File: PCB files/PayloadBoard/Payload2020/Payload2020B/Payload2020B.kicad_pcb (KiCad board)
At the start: 2 copper layers, 50 x 150 mm, 3 parts, among them J1 BridgeConn, U1 Xbee_XBP9B, U2 BerryIMUv3

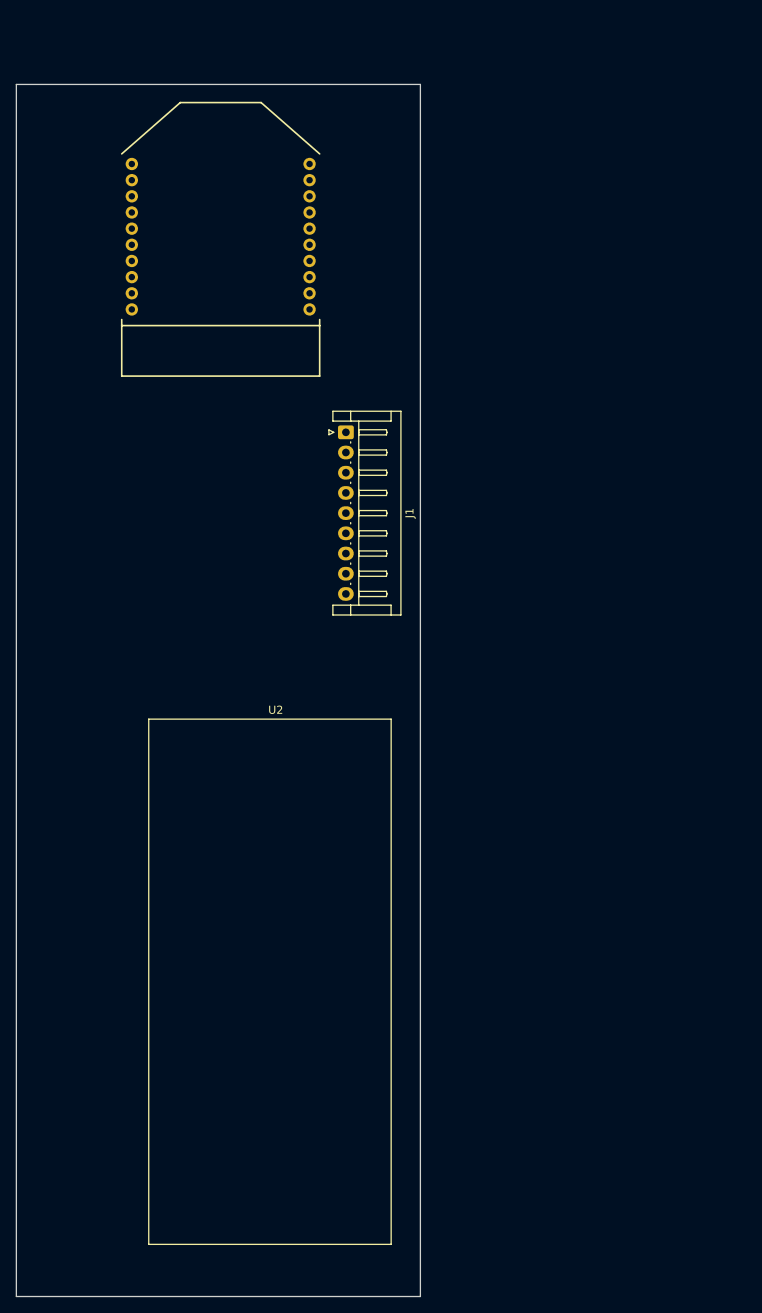
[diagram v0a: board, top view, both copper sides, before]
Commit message: Changed board sizes based on payload bay dimensions Changed battery connector to JST XH
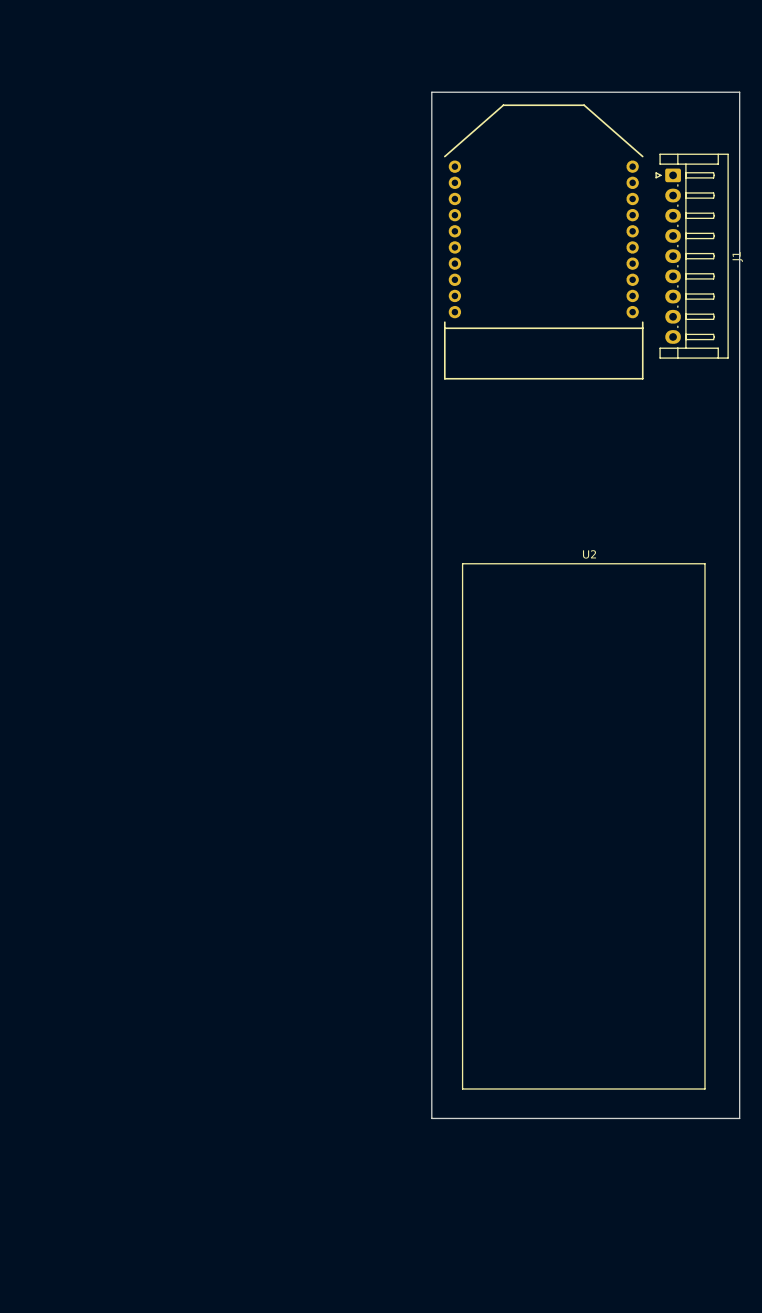
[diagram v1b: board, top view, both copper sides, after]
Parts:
- moved J1 51.5 mm to (149.7, 42.0)
- moved U2 43.3 mm to (139.6, 124.0)
- moved U1 40.0 mm to (133.7, 60.9)
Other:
- board size 50 x 150 mm -> 38.1 x 127 mm
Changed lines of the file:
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@@
     (solder_mask_min_width 0.25)
     (aux_axis_origin 0 0)
-    (visible_elements FFFFFF7F)
+    (visible_elements 7FFFFFFF)
     (pcbplotparams
       (layerselection 0x010fc_ffffffff)
@@
   )
   (module Connector_JST:JST_EH_S9B-EH_1x09_P2.50mm_Horizontal (layer F.Cu)
-    (at 109.22 73.787 270)
+    (at 149.71014 41.9862 270)
     (descr "JST EH series connector, S9B-EH (http://www.jst-mfg.com/product/pdf/eng/eEH.pdf), generated with kicad-footprint-generator")
     (tags "connector JST EH horizontal")
@@
   )
   (module SparkFunRF:XBEE-1 (layer F.Cu)
-    (at 93.726 60.579)
+    (at 133.70814 60.9092)
     (attr virtual)
     (fp_text reference U1 (at -7.874 -2.7432) (layer B.SilkS)
@@
   )
   (module Payload:BerryGPS-IMU_V3 (layer F.Cu)
-    (at 100.711 143.256)
+    (at 139.55014 124.0282)
     (fp_text reference U2 (at -0.17272 -35.09772) (layer F.SilkS)
       (effects (font (size 1 1) (thickness 0.15)))
@@
     (fp_line (start -15.89024 31.02496) (end 14.10976 31.02496) (layer F.SilkS) (width 0.12))
   )
-  (gr_line (start 68.438 30.734) (end 68.438 180.734) (layer Edge.Cuts) (width 0.05))
-  (gr_line (start 118.438 180.734) (end 118.438 30.734) (layer Edge.Cuts) (width 0.05))
-  (gr_line (start 68.438 180.734) (end 118.438 180.734) (layer Edge.Cuts) (width 0.05))
-  (gr_line (start 68.438 30.734) (end 118.438 30.734) (layer Edge.Cuts) (width 0.05))
+  (gr_line (start 119.85014 31.6992) (end 119.85014 158.6992) (layer Edge.Cuts) (width 0.05))
+  (gr_line (start 157.95014 158.6992) (end 157.95014 31.6992) (layer Edge.Cuts) (width 0.05))
+  (gr_line (start 119.85014 158.6992) (end 157.95014 158.6992) (layer Edge.Cuts) (width 0.05))
+  (gr_line (start 119.85014 31.6992) (end 157.95014 31.6992) (layer Edge.Cuts) (width 0.05))
 )

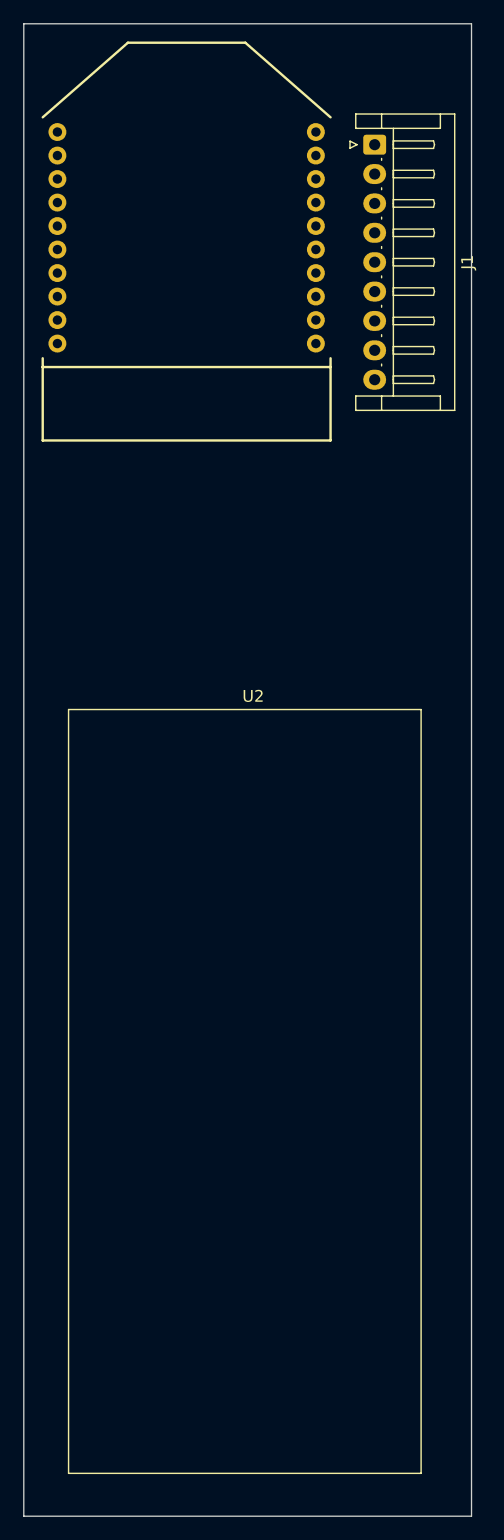
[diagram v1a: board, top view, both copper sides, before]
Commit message: -Selected all footprints -Began routing Board A
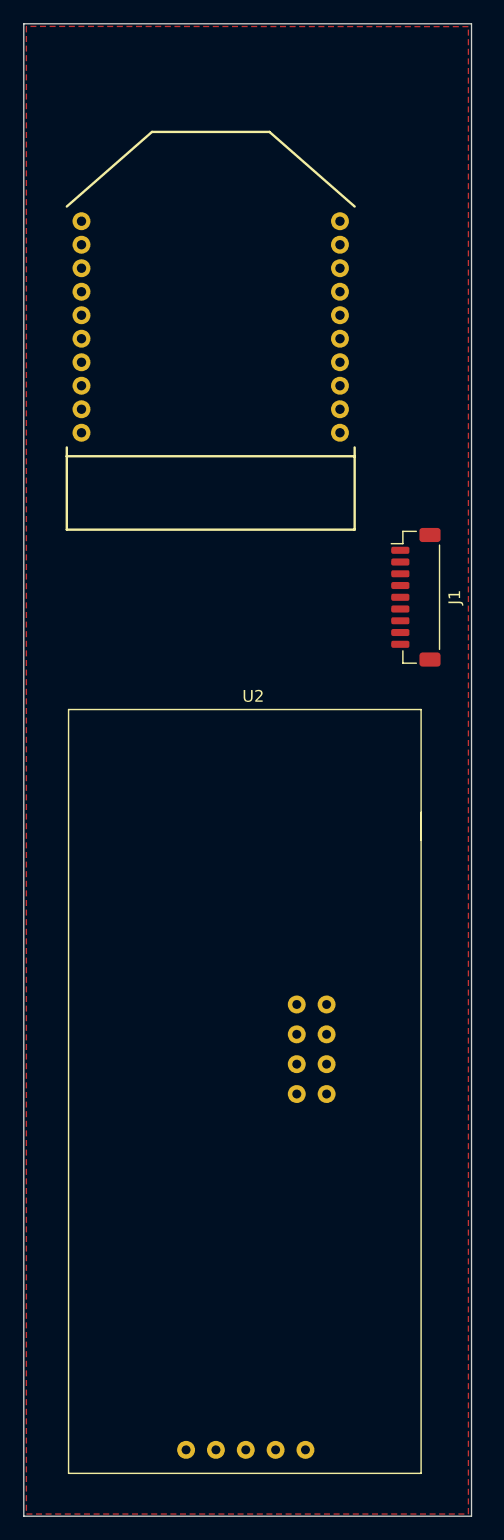
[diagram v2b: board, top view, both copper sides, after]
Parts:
- J1: footprint Connector_JST:JST_EH_S9B-EH_1x09_P2.50mm_Horizontal -> Connector_JST:JST_SH_BM09B-SRSS-TB_1x09-1MP_P1.00mm_Vertical
- moved J1 38.7 mm to (153.2, 80.5)
- moved U1 7.86 mm to (135.8, 68.5)
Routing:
- added copper zone on F.Cu, net GNDREF

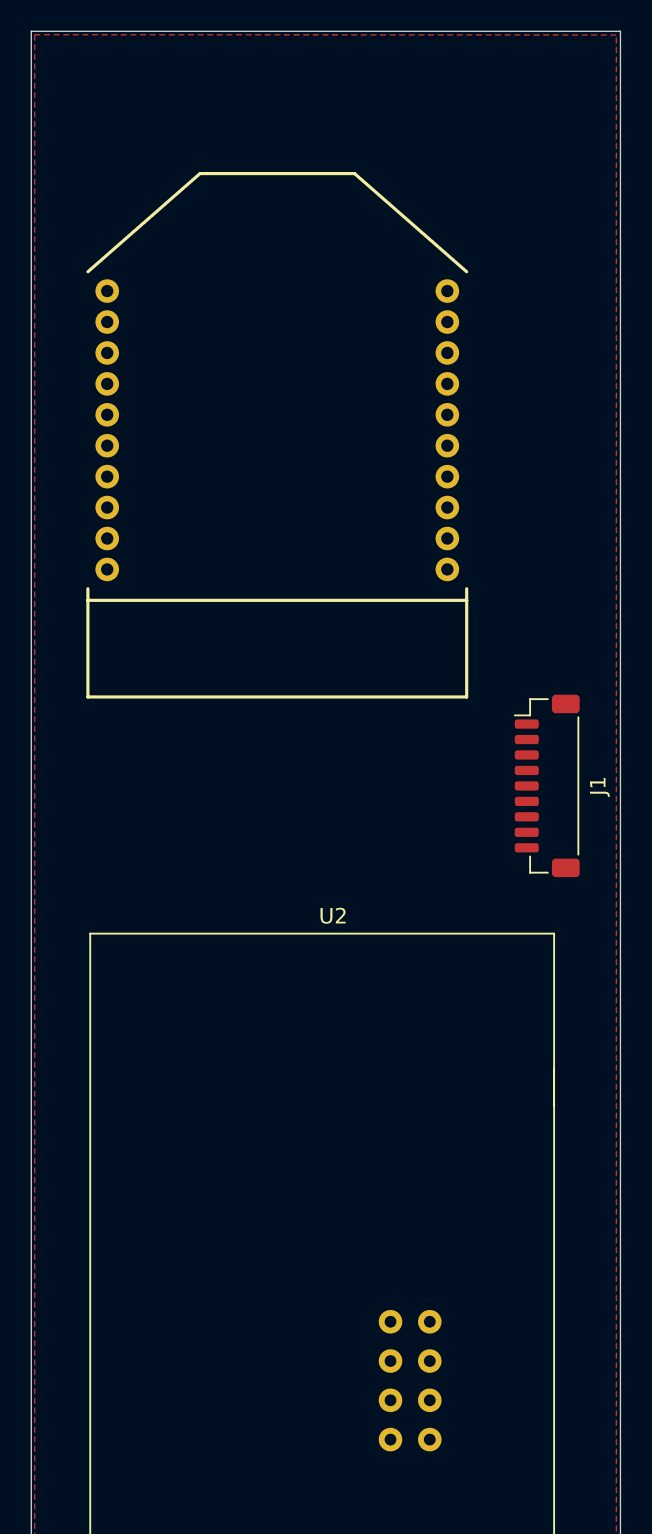
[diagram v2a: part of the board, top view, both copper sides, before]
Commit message: Began routing Board B Adjusted board bridge to 10 pins to transfer both 3.3v rails
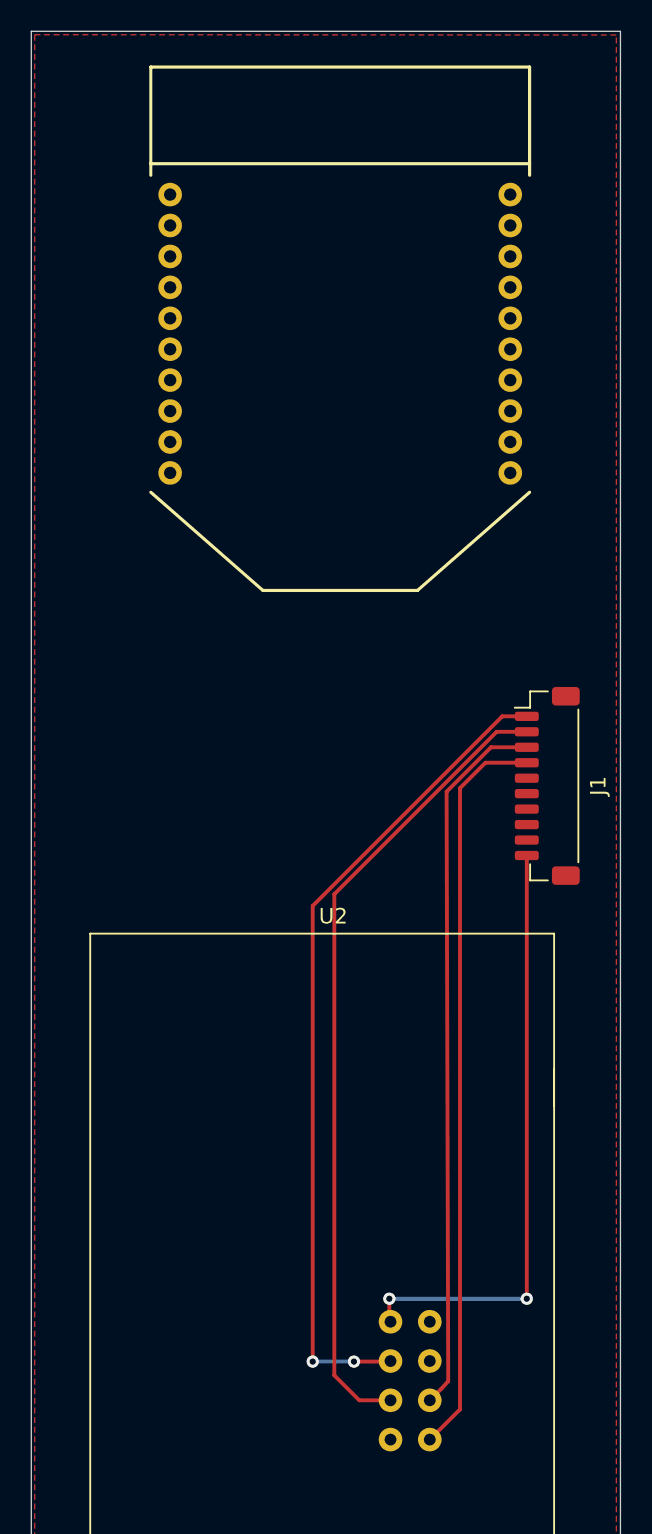
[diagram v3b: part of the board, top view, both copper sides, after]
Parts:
- J1: footprint Connector_JST:JST_SH_BM09B-SRSS-TB_1x09-1MP_P1.00mm_Vertical -> Connector_JST:JST_SH_BM10B-SRSS-TB_1x10-1MP_P1.00mm_Vertical
- moved U1 28.5 mm to (139.8, 40.3), turned to 180 degrees
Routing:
- net /Berry_SDA: track 0.00 -> 53.4 mm, vias 0 -> 2
- net /Berry_SCL: track 0.00 -> 52.2 mm
- net /TX_GPS: track 0.00 -> 47.9 mm
- net /RX_GPS: track 0.00 -> 46.2 mm
- net +3V3: track 0.00 -> 39.1 mm, vias 0 -> 2
